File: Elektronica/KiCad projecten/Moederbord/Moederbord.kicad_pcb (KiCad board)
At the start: 2 copper layers, 150 x 150 mm, 56 parts, among them J1 Conn_02x06_Odd_Even, J10 Conn_01x06_Male, J11 Conn_01x06_Male, J12 Conn_01x06_Male, J13 Conn_01x06_Male, J14 Conn_01x06_Male, J15 Conn_01x06_Male, J16 Conn_01x06_Male, J17 Conn_01x06_Male, J18 Conn_01x06_Male, J19 Conn_01x06_Male, J2 I2S_DAC, J20 Conn_01x06_Male, J21 Conn_01x06_Male, J22 Conn_01x06_Male, J23 Conn_01x06_Male, J24 Conn_01x06_Male, J25 Conn_01x06_Male, J26 Conn_01x06_Male, J27 Conn_01x06_Male, J28 Conn_01x06_Male, J29 Conn_01x06_Male, J3 Conn_02x02_Top_Bottom, J30 Conn_01x06_Male, J31 Conn_01x06_Male, J32 Conn_01x06_Male, J33 Conn_01x06_Male, J34 Conn_01x06_Male, J35 Conn_02x08_Odd_Even, J36 Conn_02x08_Odd_Even, J37 Conn_02x08_Odd_Even, J38 Conn_01x03, J39 Conn_01x03, J4 Screw_Terminal_01x02, J40 Conn_02x12_Odd_Even, J41 Conn_02x12_Odd_Even, J5 Conn_02x06_Odd_Even, J6 Conn_01x06_Female, J7 Conn_01x12_Female, J8 Conn_01x12_Female, J9 Screw_Terminal_01x02, U1 74166, U2 74166, U3 74166

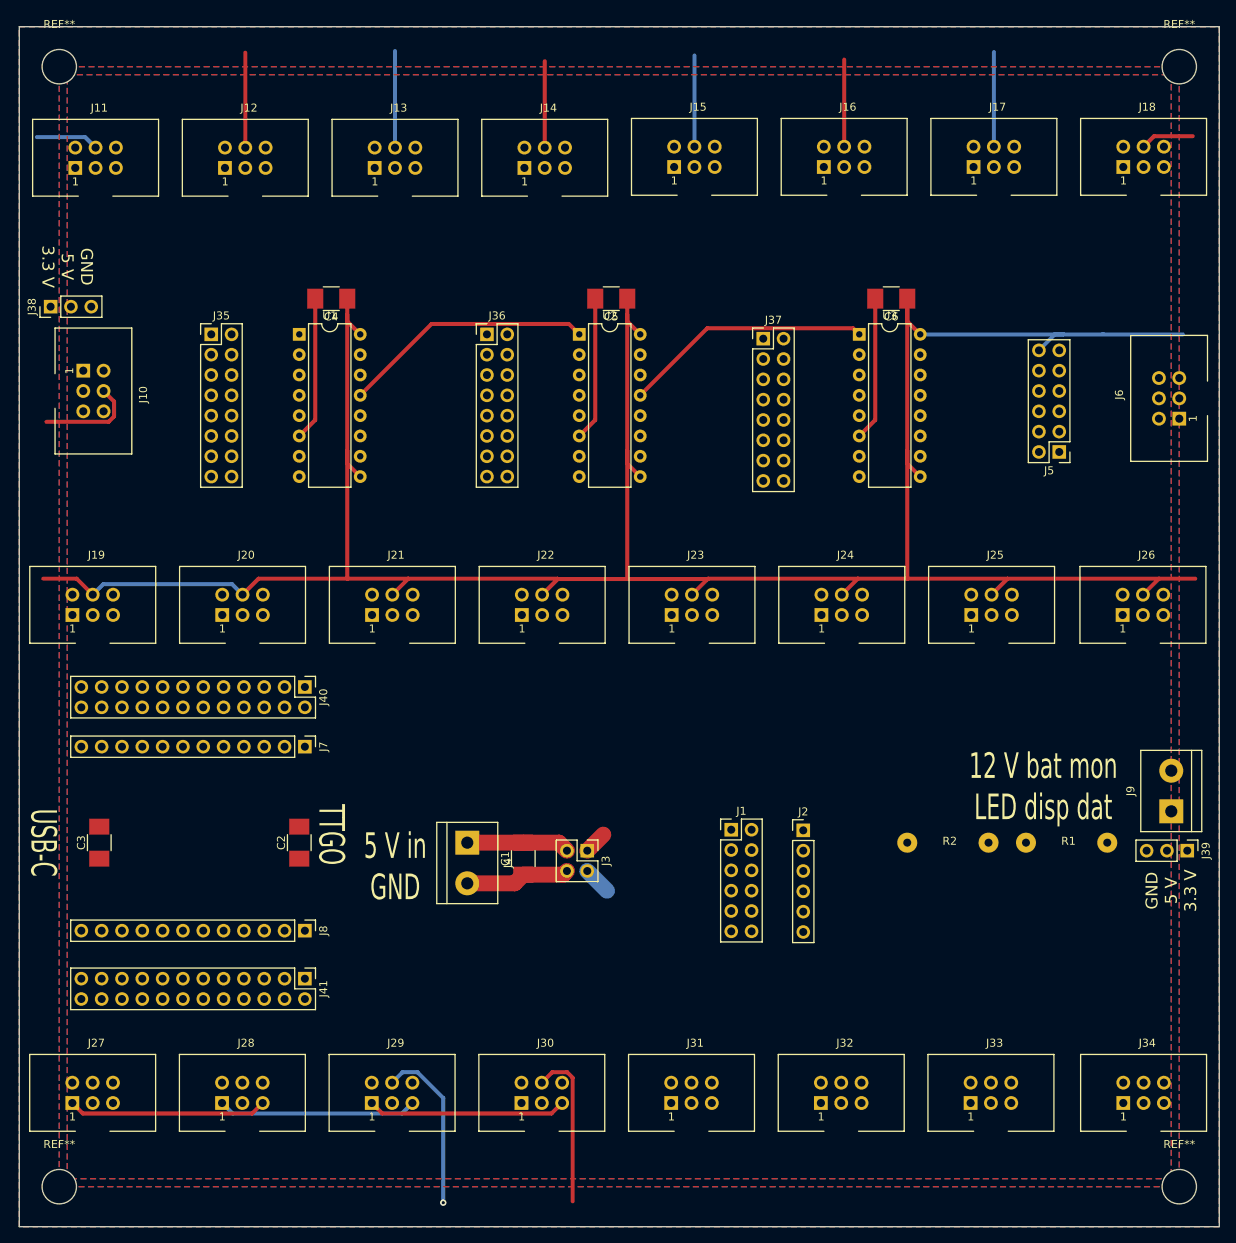
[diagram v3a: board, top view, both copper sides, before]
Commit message: Update vanwege 25e toets (dus nu 26 toetsmodules met menu-knop)
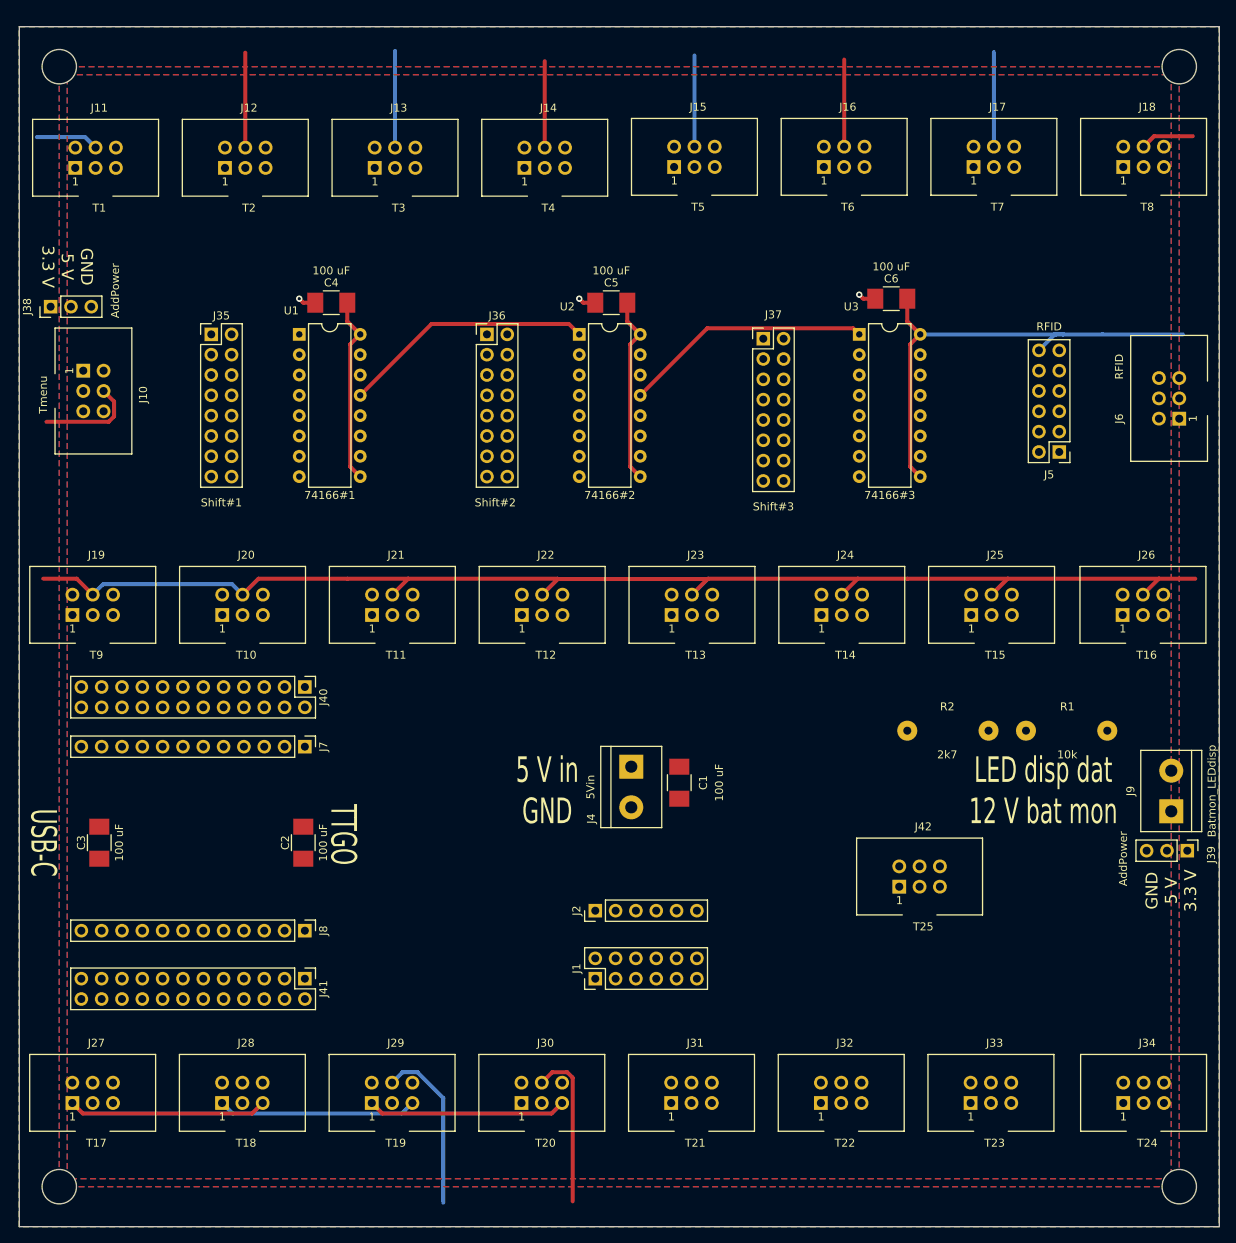
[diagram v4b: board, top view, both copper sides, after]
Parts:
- removed J3: Conn_02x02_Top_Bottom, Pin_Headers:Pin_Header_Straight_2x02_Pitch2.54mm
- added J42: T25, Moederbord:IDC_Header_Straight_6pins, F.Cu at (133.0, 134.5)
- J1: value Conn_02x06_Odd_Even -> I2S_DAC
- J10: value Conn_01x06_Male -> Tmenu
- J11: value Conn_01x06_Male -> T1
- J12: value Conn_01x06_Male -> T2
- J13: value Conn_01x06_Male -> T3
- J14: value Conn_01x06_Male -> T4
- J15: value Conn_01x06_Male -> T5
- J16: value Conn_01x06_Male -> T6
- J17: value Conn_01x06_Male -> T7
- J18: value Conn_01x06_Male -> T8
- J19: value Conn_01x06_Male -> T9
- J20: value Conn_01x06_Male -> T10
- J21: value Conn_01x06_Male -> T11
- J22: value Conn_01x06_Male -> T12
- J23: value Conn_01x06_Male -> T13
- J24: value Conn_01x06_Male -> T14
- J25: value Conn_01x06_Male -> T15
- J26: value Conn_01x06_Male -> T16
- J27: value Conn_01x06_Male -> T17
- J28: value Conn_01x06_Male -> T18
- J29: value Conn_01x06_Male -> T19
- J30: value Conn_01x06_Male -> T20
- J31: value Conn_01x06_Male -> T21
- J32: value Conn_01x06_Male -> T22
- J33: value Conn_01x06_Male -> T23
- J34: value Conn_01x06_Male -> T24
- J35: value Conn_02x08_Odd_Even -> Shift#1
- J36: value Conn_02x08_Odd_Even -> Shift#2
- J37: value Conn_02x08_Odd_Even -> Shift#3
- J38, J39: value Conn_01x03 -> AddPower
- J4: value Screw_Terminal_01x02 -> 5Vin
- J40: value Conn_02x12_Odd_Even -> uCleft
- J41: value Conn_02x12_Odd_Even -> uCright
- J5: value Conn_02x06_Odd_Even -> RFID
- J6: value Conn_01x06_Female -> RFID
- J9: value Screw_Terminal_01x02 -> Batmon_LEDdisp
- U1: value 74166 -> 74166#1
- U2: value 74166 -> 74166#2
- U3: value 74166 -> 74166#3
- moved J2 27.9 mm to (95.0, 137.5), turned to 90 degrees
- moved J1 25.2 mm to (95.0, 146.0), turned to 90 degrees
- moved J4 22.6 mm to (99.5, 119.5)
- moved C1 21.7 mm to (105.5, 121.5)
- moved R1 14.0 mm to (159.0, 115.0)
- moved R2 14.0 mm to (144.2, 115.0)
- moved C2 0.50 mm to (58.5, 129.0)
- moved C4 0.50 mm to (62.0, 61.5)
- moved C5 0.50 mm to (97.0, 61.5)
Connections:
- net Net-(J9-Pad1) renamed /Vbat12V
- C1 pad 1: /Conn_GND -> GND
- C1 pad 2: /Conn_5V -> +5V
- J34 pad 1: (no net) -> /Toetsmodules/LED24_LED25
- J4 pad 1: /Conn_5V -> +5V
- J4 pad 2: /Conn_GND -> GND
- J40 pad 11: Shift_SH_LDn3 -> (no net)
- J40 pad 7: Shift_SH_LDn1 -> Shift_SH_LDn
- J40 pad 9: Shift_SH_LDn2 -> Touch25
- U1 pad 15: Shift_SH_LDn1 -> Shift_SH_LDn
- U2 pad 15: Shift_SH_LDn2 -> Shift_SH_LDn
- U3 pad 15: Shift_SH_LDn3 -> Shift_SH_LDn
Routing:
- net +3V3: track 466.0 -> 408.6 mm, vias 1 -> 0
- net GND: track 57.4 -> 6.62 mm, vias 0 -> 3
- net /Conn_GND: track 13.1 -> 0.00 mm
- net /Conn_5V: track 12.9 -> 0.00 mm
- net +5V: track 2.83 -> 0.00 mm
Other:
- board text added: "LED disp dat 12 V bat mon"
- board text removed: "12 V bat mon LED disp dat"

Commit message: Update moederbord
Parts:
- moved J39 6.50 mm to (169.0, 136.5)
- moved C1 2.50 mm to (108.0, 121.5)
- moved R2 1.34 mm to (145.5, 115.0)
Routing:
- net +3V3: track 408.6 -> 597.5 mm, vias 0 -> 4
- net +5V: track 0.00 -> 87.9 mm
- net /Shift registers/T24: track 0.00 -> 34.4 mm
- net /Shift registers/T16: track 0.00 -> 33.2 mm
- net /Shift registers/T8: track 0.00 -> 32.7 mm
- net GND: track 6.62 -> 36.5 mm, vias 3 -> 2
- net /Shift registers/T23: track 0.00 -> 25.3 mm
- net /Toetsmodules/LED23_LED24: track 0.00 -> 25.3 mm
- net /Toetsmodules/LED22_LED23: track 0.00 -> 24.8 mm
- net /Toetsmodules/LED20_LED21: track 0.00 -> 24.8 mm
- net /Toetsmodules/LED21_LED22: track 0.00 -> 24.8 mm
- net /Shift registers/T15: track 0.00 -> 24.7 mm
- net /Shift registers/T7: track 0.00 -> 24.1 mm
- net /Shift registers/T22: track 0.00 -> 23.3 mm
- net /Shift registers/T14: track 0.00 -> 23.1 mm
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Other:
- board text added: "3.3 V 5 V GND"

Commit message: Eerste versie van moederbord klaar
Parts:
- removed REF** (x3): MountingHole_4.3mm_M4, Mounting_Holes:MountingHole_4.3mm_M4
- added X2: MountingHole_4.3mm_M4, Mounting_Holes:MountingHole_4.3mm_M4, F.Cu at (168.0, 32.0)
- added X3: MountingHole_4.3mm_M4, Mounting_Holes:MountingHole_4.3mm_M4, F.Cu at (28.0, 172.0)
- added X4: MountingHole_4.3mm_M4, Mounting_Holes:MountingHole_4.3mm_M4, F.Cu at (168.0, 172.0)
- J7: value Conn_01x12_Female -> uCleft
- J8: value Conn_01x12_Female -> uCright
- R1: value 10k -> 100k
- R2: value 2k7 -> 10k
- renumbered REF** to X1
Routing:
- net GND: track 36.5 -> 907.5 mm, vias 2 -> 0
- net +5V: track 87.9 -> 780.4 mm, vias 0 -> 1
- net +3V3: track 597.5 -> 889.9 mm, vias 4 -> 1
- net /Toetsmodules/LED16_LED17: track 0.00 -> 167.4 mm
- net RFID_MISO: track 0.00 -> 158.2 mm, vias 0 -> 1
- net Touch8: track 0.00 -> 157.6 mm, vias 0 -> 1
- net Touch17: track 0.00 -> 155.5 mm, vias 0 -> 1
- net /Toetsmodules/LED8_LED9: track 0.00 -> 151.4 mm, vias 0 -> 2
- net Shift_SH_LDn: track 0.00 -> 149.8 mm
- net LED_display_data: track 0.00 -> 149.1 mm
- net Shift_data: track 0.00 -> 139.6 mm, vias 0 -> 1
- net RFID_CS: track 0.00 -> 136.4 mm, vias 0 -> 1
- net Touch18: track 0.00 -> 134.9 mm
- net RFID_MOSI: track 0.00 -> 126.7 mm, vias 0 -> 2
- net RFID_SCLK: track 0.00 -> 126.3 mm, vias 0 -> 2
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- removed copper zone on B.Cu, net +3V3
- removed copper zone on F.Cu, net +3V3
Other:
- board text added: "BCK DATA LRCK GND GND VCC=5V"
- board text added: "Moederbord v1 2022-01 WvdP"
